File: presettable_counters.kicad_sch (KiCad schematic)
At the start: 13 parts

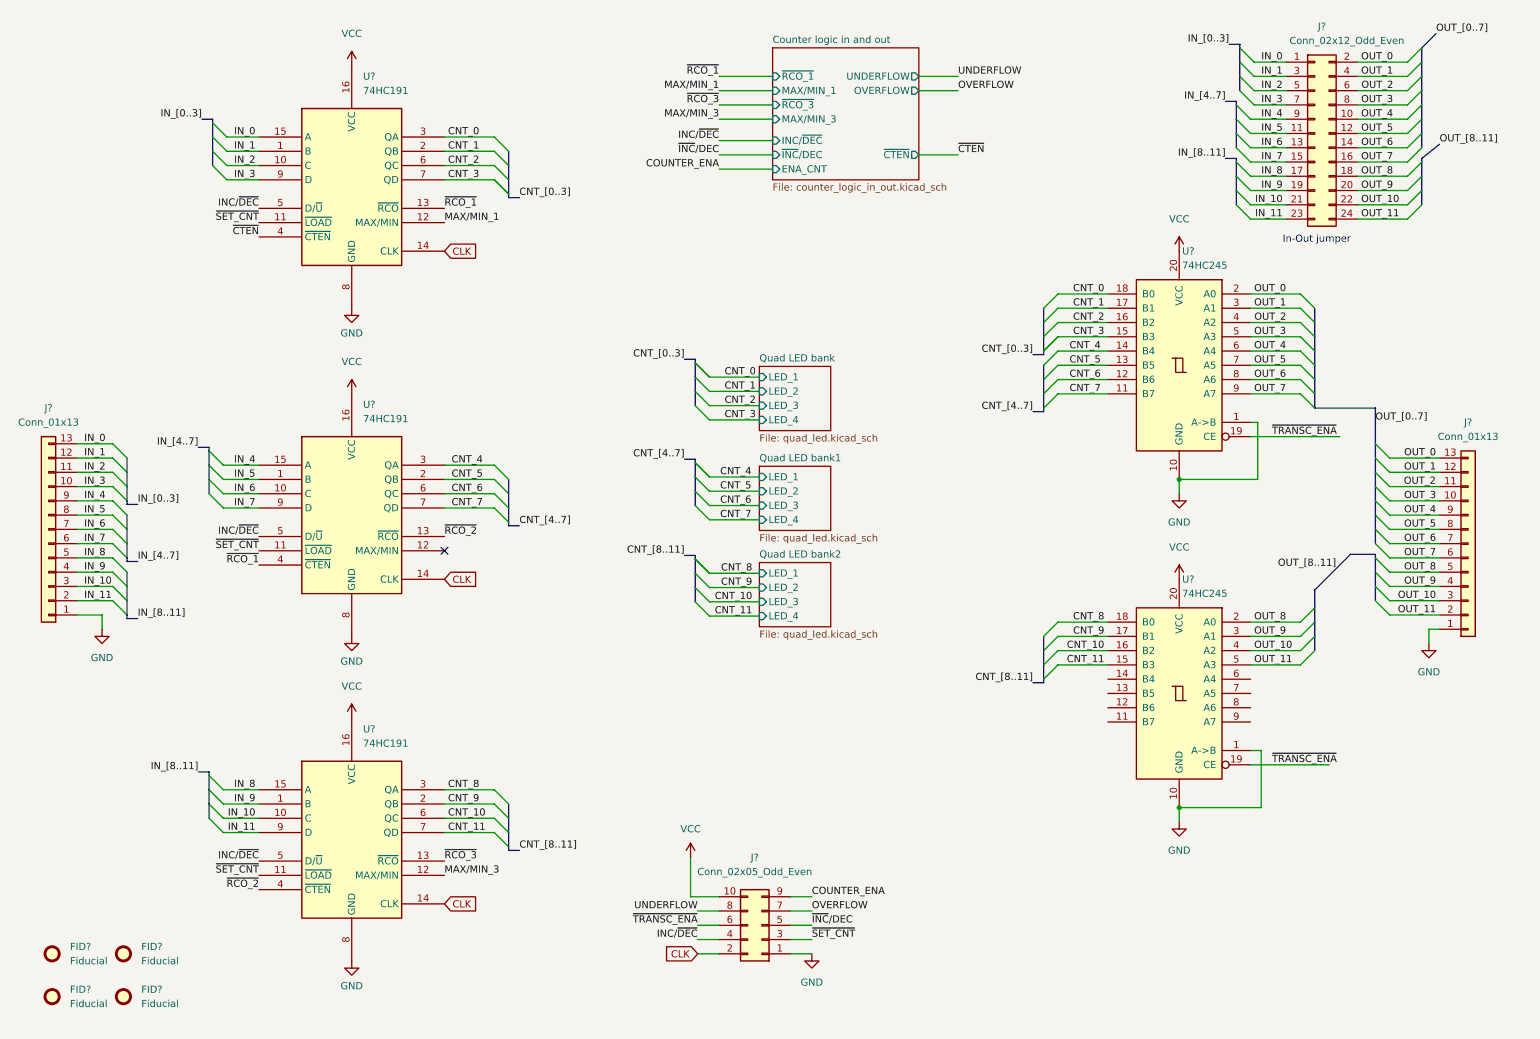
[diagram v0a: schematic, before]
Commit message: Review fixes
- swapped to HC components
- removed ctn_enable
- all 12 LEDs merged into 1 sheet
- No more error with the electrical checker
- various style improvements
- Introduce sleep deprivation errors like calling tranceivers d flip flops
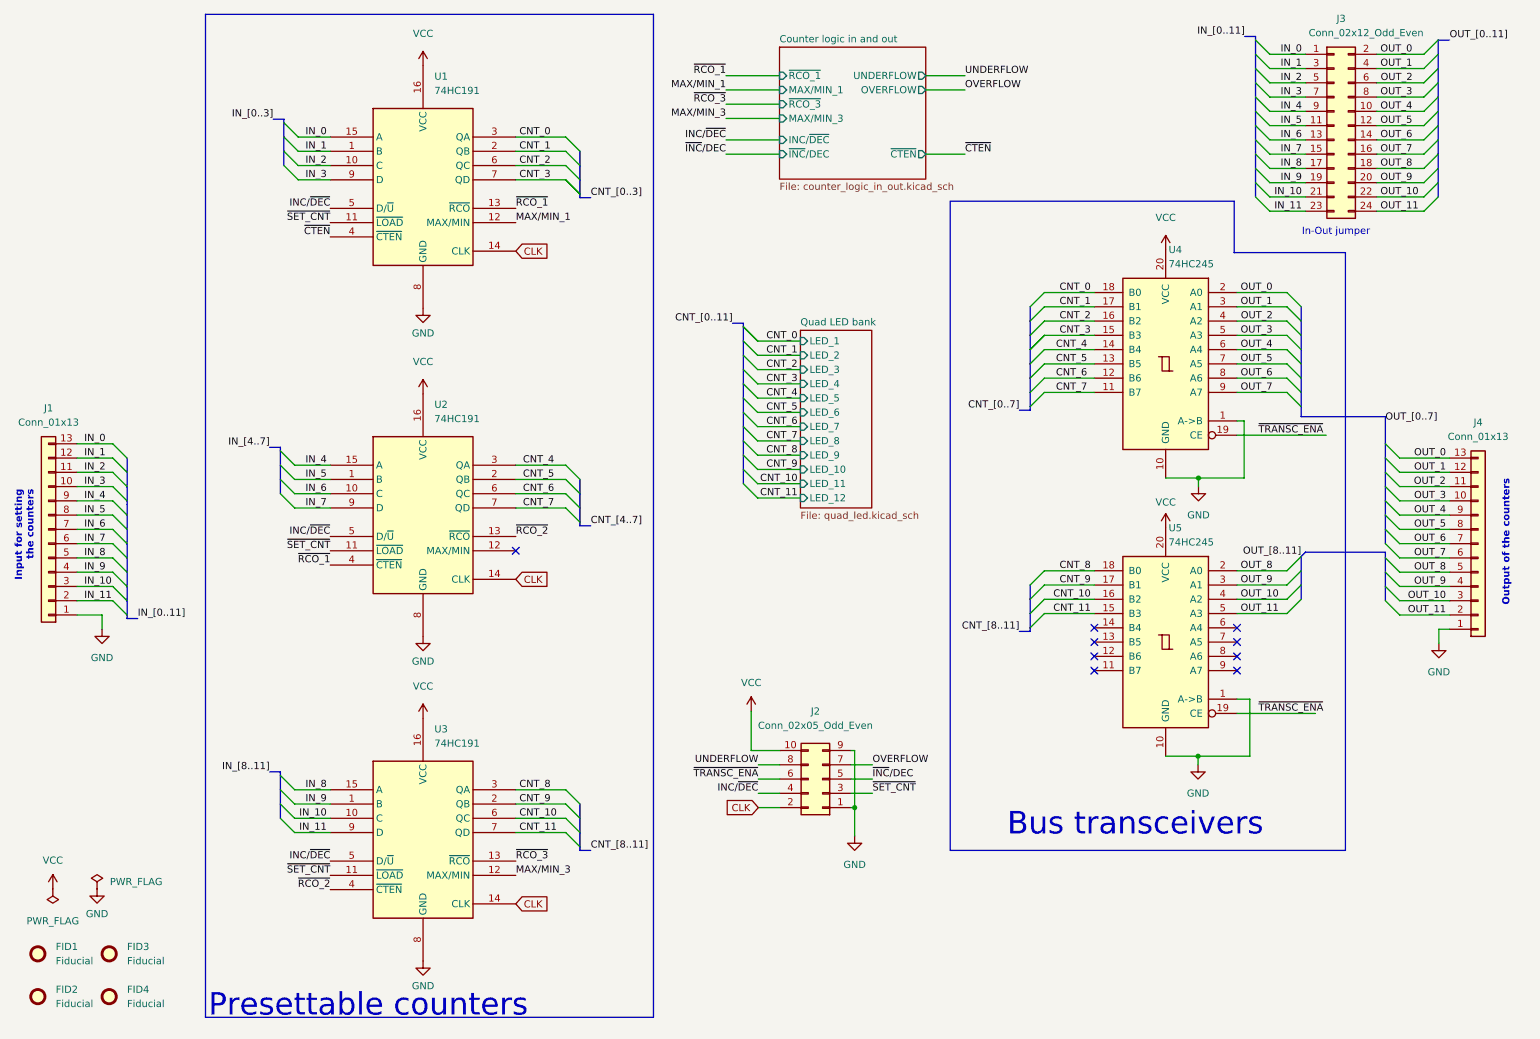
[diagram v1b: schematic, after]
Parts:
- J2: renamed from J?; footprint (none) -> Connector_PinHeader_2.54mm:PinHeader_2x05_P2.54mm_Vertical
- J3: renamed from J?; footprint (none) -> Connector_PinHeader_2.54mm:PinHeader_2x12_P2.54mm_Vertical
- U1, U2, U3: renamed from U?; footprint (none) -> Package_SO:SOIC-16_3.9x9.9mm_P1.27mm
- U5: renamed from U?; footprint (none) -> footprints:TSSOP20B-M
- gave numbers to parts that had none: 7
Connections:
- net COUNTER_ENA is gone; now on net GND: J2.9 (Pin_9)
- no-connect marks 1 -> 9
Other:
- removed sheet Quad LED bank1
- removed sheet Quad LED bank2
- sheet Counter logic in and out ports: added none; removed ENA_CNT
- sheet Quad LED bank ports: added LED_10, LED_11, LED_12, LED_5, LED_6, LED_7, LED_8, LED_9; removed none
- note added: "Bus transceivers"
- note added: "Input for setting the counters"
- note added: "Output of the counters"
- note added: "Presettable counters"
- moved on the sheet: FID1, FID2, FID3, FID4, J2, J3, J4, U1, U2, U3, U4, U5

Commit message: Trace the layout
- Place components on PCB
- Add silkscreeen
- Add traces
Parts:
- added C1, C2, C3: 100nF, symbol Device:C
- added C4, C5, C6: C_0603_1608Metric_Pad1.08x0.95mm_HandSolder, Capacitor_SMD:C_0603_1608Metric_Pad1.08x0.95mm_HandSolder, symbol Device:C
- added J10, J11, J12, J13, J14, J15, J5, J6, J7, J8, J9: Conn_02x12_Odd_Even, Jumper:SolderJumper-2_P1.3mm_Open_RoundedPad1.0x1.5mm, symbol Jumper:SolderJumper_2_Open
- FID1, FID2, FID3, FID4: footprint (none) -> Fiducial:Fiducial_1.5mm_Mask3mm
- J3: footprint Connector_PinHeader_2.54mm:PinHeader_2x12_P2.54mm_Vertical -> Jumper:SolderJumper-2_P1.3mm_Open_RoundedPad1.0x1.5mm; symbol Connector_Generic:Conn_02x12_Odd_Even -> Jumper:SolderJumper_2_Open
- U4, U5: footprint footprints:TSSOP20B-M -> Package_SO:SOIC-20W_7.5x12.8mm_P1.27mm
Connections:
- net CNT_0: now also U4.2 (A0); no longer U4.18 (B0)
- net CNT_1: now also U4.3 (A1); no longer U4.17 (B1)
- net CNT_10: now also U5.4 (A2); no longer U5.16 (B2)
- net CNT_11: now also U5.5 (A3); no longer U5.15 (B3)
- net CNT_2: now also U4.4 (A2); no longer U4.16 (B2)
- net CNT_3: now also U4.5 (A3); no longer U4.15 (B3)
- net CNT_4: now also U4.6 (A4); no longer U4.14 (B4)
- net CNT_5: now also U4.7 (A5); no longer U4.13 (B5)
- net CNT_6: now also U4.8 (A6); no longer U4.12 (B6)
- net CNT_7: now also U4.9 (A7); no longer U4.11 (B7)
- net CNT_8: now also U5.2 (A0); no longer U5.18 (B0)
- net CNT_9: now also U5.3 (A1); no longer U5.17 (B1)
- net GND: now also C1.2, C2.2, C3.2, C4.1, C5.1, C6.1; no longer U4.1 (A->B), U5.1 (A->B)
- net IN_1: now also J5.1 (A); no longer J3.3 (Pin_3)
- net IN_10: now also J14.1 (A); no longer J3.21 (Pin_21)
- net IN_11: now also J15.1 (A); no longer J3.23 (Pin_23)
- net IN_2: now also J6.1 (A); no longer J3.5 (Pin_5)
- net IN_3: now also J7.1 (A); no longer J3.7 (Pin_7)
- net IN_4: now also J8.1 (A); no longer J3.9 (Pin_9), U2.15 (A)
- net IN_5: now also J9.1 (A); no longer J3.11 (Pin_11)
- net IN_6: now also J10.1 (A); no longer J3.13 (Pin_13)
- net IN_7: now also J11.1 (A); no longer J3.15 (Pin_15)
- net IN_8: now also J12.1 (A); no longer J3.17 (Pin_17)
- net IN_9: now also J13.1 (A); no longer J3.19 (Pin_19)
- net OUT_0: now also U4.18 (B0); no longer U4.2 (A0)
- net OUT_1: now also U4.17 (B1), J5.2 (B); no longer J3.4 (Pin_4), U4.3 (A1)
- net OUT_10: now also U5.16 (B2), J14.2 (B); no longer J3.22 (Pin_22), U5.4 (A2)
- net OUT_11: now also U5.15 (B3), J15.2 (B); no longer J3.24 (Pin_24), U5.5 (A3)
- net OUT_2: now also U4.16 (B2), J6.2 (B); no longer J3.6 (Pin_6), U4.4 (A2)
- net OUT_3: now also U4.15 (B3), J7.2 (B); no longer J3.8 (Pin_8), U4.5 (A3)
- net OUT_4: now also U4.14 (B4), J8.2 (B); no longer J3.10 (Pin_10), U4.6 (A4)
- net OUT_5: now also U4.13 (B5), J9.2 (B); no longer J3.12 (Pin_12), U4.7 (A5)
- net OUT_6: now also U4.12 (B6), J10.2 (B); no longer J3.14 (Pin_14), U4.8 (A6)
- net OUT_7: now also U4.11 (B7), J11.2 (B); no longer J3.16 (Pin_16), U4.9 (A7)
- net OUT_8: now also U5.18 (B0), J12.2 (B); no longer J3.18 (Pin_18), U5.2 (A0)
- net OUT_9: now also U5.17 (B1), J13.2 (B); no longer J3.20 (Pin_20), U5.3 (A1)
- net VCC: now also U4.1 (A->B), U5.1 (A->B), C1.1, C2.1, C3.1, C4.2, C5.2, C6.2
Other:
- moved on the sheet: J2, U1, U2

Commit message: routed and pretty
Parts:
- C1, C2, C3: footprint (none) -> Capacitor_SMD:C_0603_1608Metric_Pad1.08x0.95mm_HandSolder
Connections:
- net CLK: now also J2.8 (Pin_8); no longer J2.2 (Pin_2)
- net IN_4: now also U2.15 (A)
- net UNDERFLOW: now also J2.2 (Pin_2); no longer J2.8 (Pin_8)
- net ~{INC}/DEC: now also J2.6 (Pin_6); no longer J2.5 (Pin_5)
- net ~{TRANSC_ENA}: now also J2.5 (Pin_5); no longer J2.6 (Pin_6)
